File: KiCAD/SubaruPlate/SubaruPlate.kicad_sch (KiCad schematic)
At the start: 7 parts, among them J1 DF51A-4P-2DSA, U1 LPS28DFW

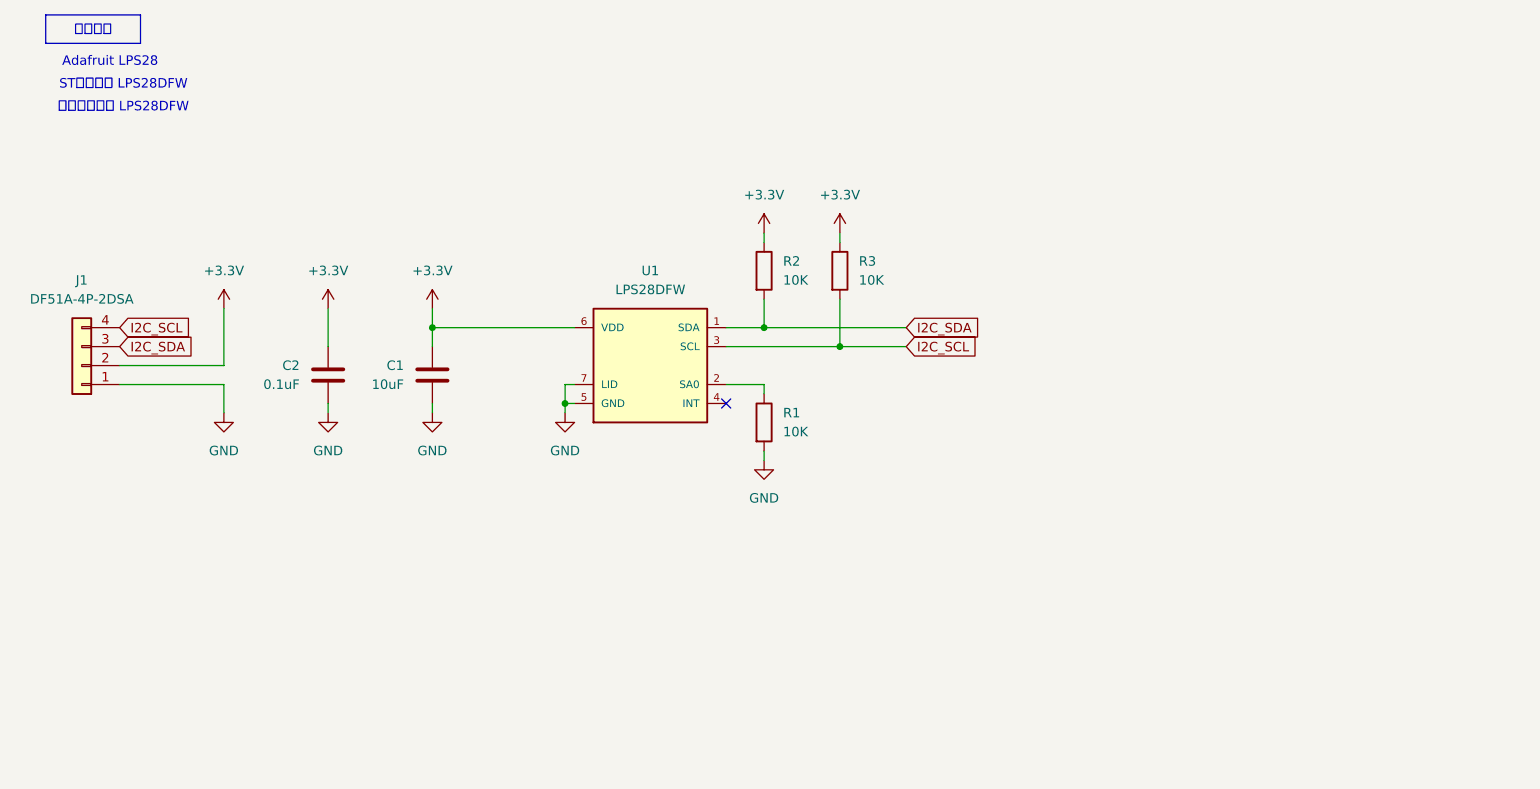
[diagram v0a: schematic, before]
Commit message: Power, CanInterface, MCU, Sensorと項目に分け設計
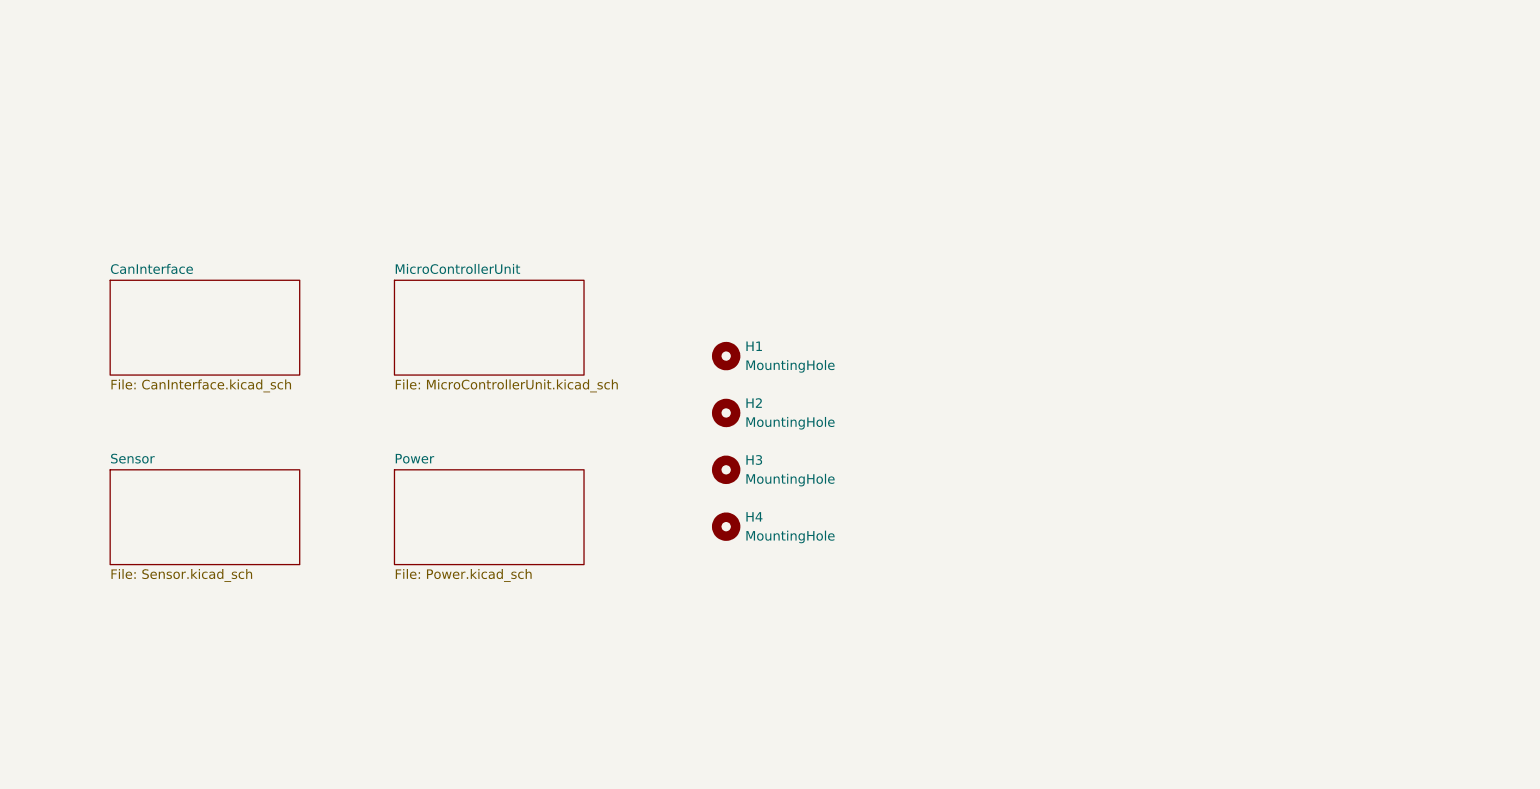
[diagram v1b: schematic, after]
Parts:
- removed C1: 10uF, Capacitor_SMD:C_0603_1608Metric_Pad1.08x0.95mm_HandSolder, symbol Device:C
- removed C2: 0.1uF, Capacitor_SMD:C_0603_1608Metric_Pad1.08x0.95mm_HandSolder, symbol Device:C
- removed J1: DF51A-4P-2DSA, TSRP_Connector_Hirose:DF51A-4P-2DSA, symbol Connector_Generic:Conn_01x04
- removed R1, R2, R3: 10K, Resistor_SMD:R_0603_1608Metric_Pad0.98x0.95mm_HandSolder, symbol Device:R
- removed U1: LPS28DFW, TSRP_IC:CCLGA-7L, symbol TSRP_IC:LPS28DFW
- added H1, H2, H3, H4: MountingHole, MountingHole:MountingHole_4.3mm_M4, symbol Mechanical:MountingHole
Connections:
- no-connect marks 1 -> 0
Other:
- added sheet CanInterface (CanInterface.kicad_sch)
- added sheet MicroControllerUnit (MicroControllerUnit.kicad_sch)
- added sheet Power (Power.kicad_sch)
- added sheet Sensor (Sensor.kicad_sch)
- note removed: "Adafruit LPS28"
- note removed: "STマイクロ LPS28DFW"
- note removed: "データシート LPS28DFW"

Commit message: SubaruPlateを更新
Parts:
- removed H1, H2, H3, H4: MountingHole, MountingHole:MountingHole_4.3mm_M4, symbol Mechanical:MountingHole
- added H5, H6, H7, H8: MountingHole_Pad, MountingHole:MountingHole_4.3mm_M4_Pad_TopBottom, symbol Mechanical:MountingHole_Pad
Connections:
- new net GND: H5.1, H6.1, H7.1, H8.1
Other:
- added sheet ServoMotor (ServoMotor.kicad_sch)

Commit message: 後は最終確認
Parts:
- H5, H6, H7, H8: footprint MountingHole:MountingHole_4.3mm_M4_Pad_TopBottom -> MountingHole:MountingHole_3.2mm_M3_Pad_TopBottom
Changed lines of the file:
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@@
 			)
 		)
-		(property "Footprint" "MountingHole:MountingHole_4.3mm_M4_Pad_TopBottom"
+		(property "Footprint" "MountingHole:MountingHole_3.2mm_M3_Pad_TopBottom"
 			(at 168.91 57.15 0)
 			(effects
@@
 			)
 		)
-		(property "Footprint" "MountingHole:MountingHole_4.3mm_M4_Pad_TopBottom"
+		(property "Footprint" "MountingHole:MountingHole_3.2mm_M3_Pad_TopBottom"
 			(at 120.65 57.15 0)
 			(effects
@@
 			)
 		)
-		(property "Footprint" "MountingHole:MountingHole_4.3mm_M4_Pad_TopBottom"
+		(property "Footprint" "MountingHole:MountingHole_3.2mm_M3_Pad_TopBottom"
 			(at 191.77 57.15 0)
 			(effects
@@
 			)
 		)
-		(property "Footprint" "MountingHole:MountingHole_4.3mm_M4_Pad_TopBottom"
+		(property "Footprint" "MountingHole:MountingHole_3.2mm_M3_Pad_TopBottom"
 			(at 144.78 57.15 0)
 			(effects

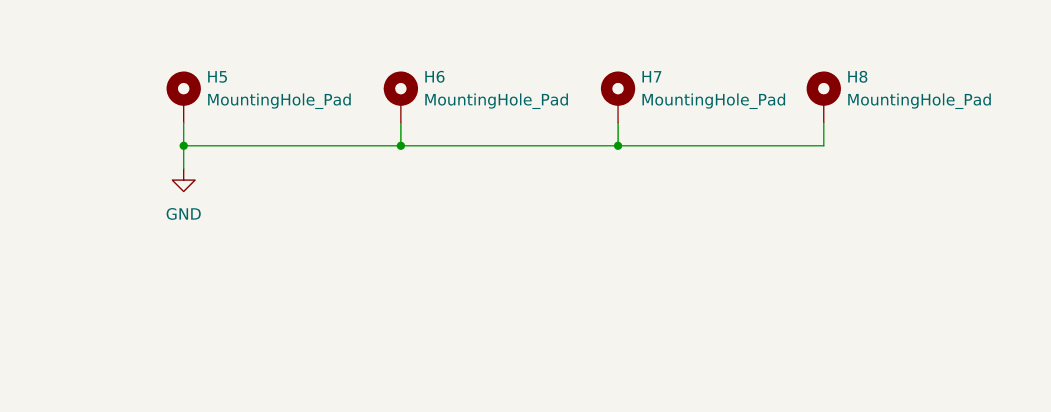
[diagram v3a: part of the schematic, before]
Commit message: 取付穴位置を変更
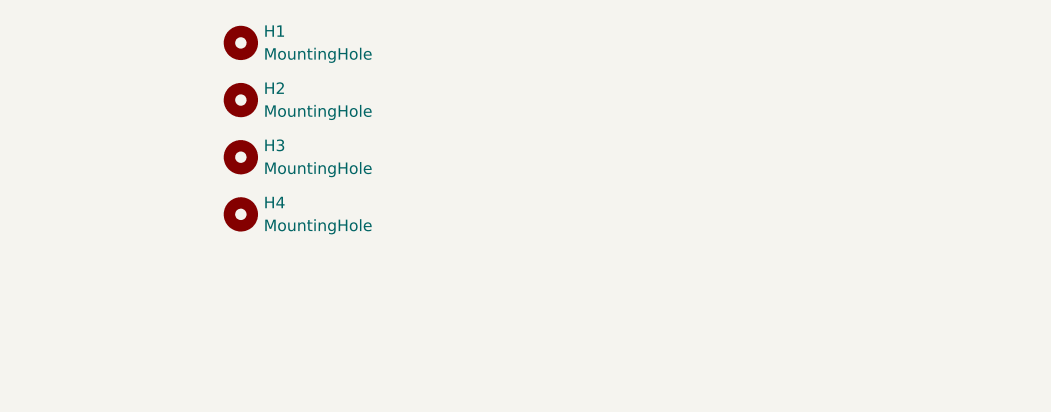
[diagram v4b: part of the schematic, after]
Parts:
- removed H5, H6, H7, H8: MountingHole_Pad, MountingHole:MountingHole_3.2mm_M3_Pad_TopBottom, symbol Mechanical:MountingHole_Pad
- added H1, H2, H3, H4: MountingHole, MountingHole:MountingHole_3.2mm_M3_Pad_TopBottom, symbol Mechanical:MountingHole

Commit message: Build-2完成．発注．
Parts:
- H1, H2, H3, H4: symbol Mechanical:MountingHole -> Mechanical:MountingHole_Pad; now in the parts list
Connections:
- new net GND: H1.1, H2.1, H3.1, H4.1
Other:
- removed sheet CanInterface
- removed sheet MicroControllerUnit
- removed sheet Power
- removed sheet ServoMotor
